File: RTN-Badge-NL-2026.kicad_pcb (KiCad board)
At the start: 2 copper layers, 85.5 x 54 mm, 152 parts, among them J1 USB_A_Edge_Connector, J2 DEBUG, J3 GPIO, SW1 BOOT, SW2 RST, SW3 USER1, SW4 USER2, U1 CH32V203F6P6, U2 ME6211C33M5, Y1 8MHz

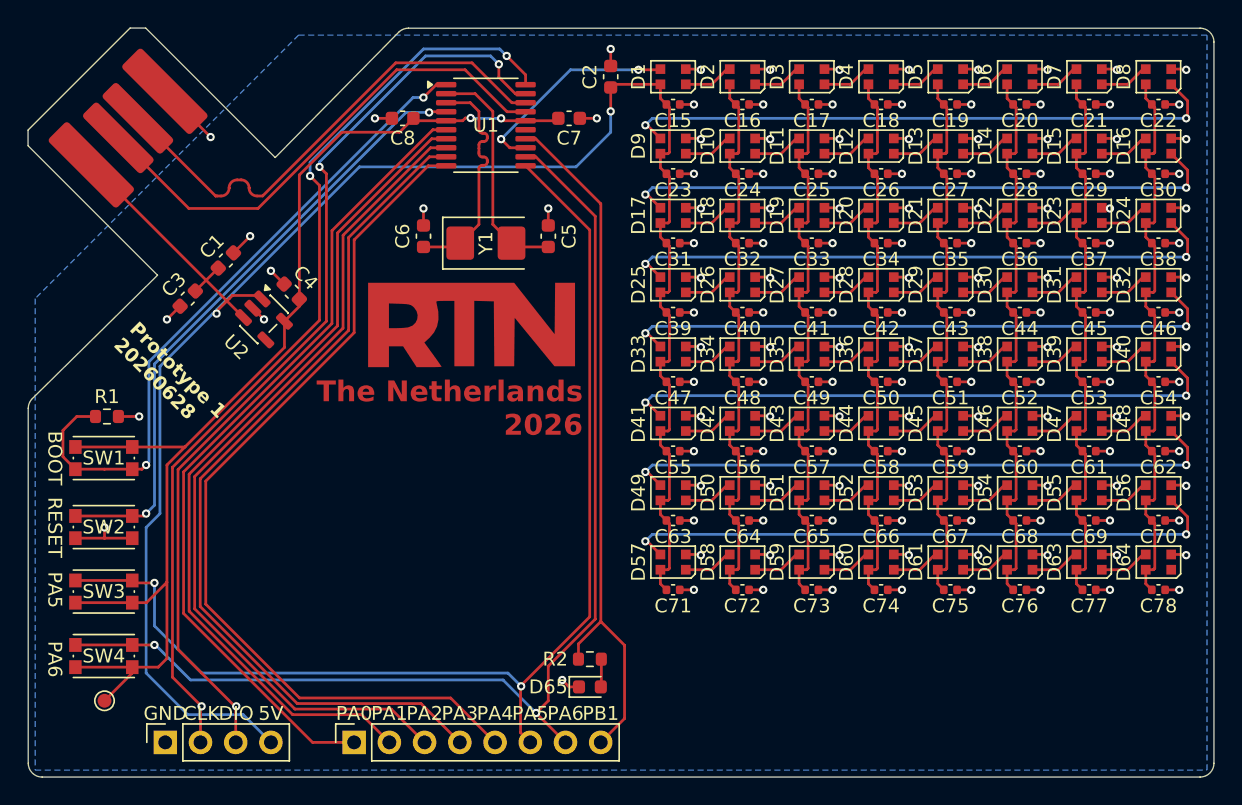
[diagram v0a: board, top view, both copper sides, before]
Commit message: Adjust PCB to use components available in JLCPCB's product library
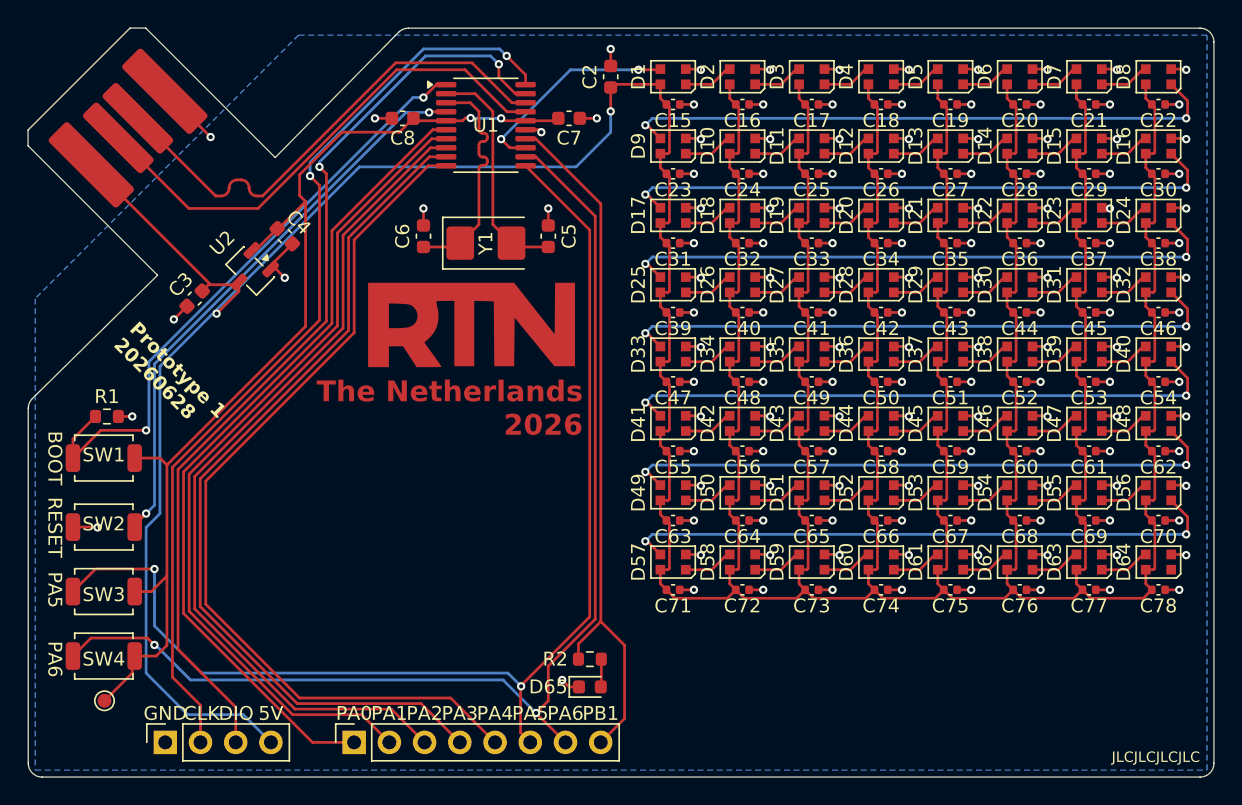
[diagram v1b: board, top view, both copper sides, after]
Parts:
- removed C1: 4.7uF or 10uF, Capacitor_SMD:C_0603_1608Metric
- C7, C8: value 20pF -> 100pF
- SW1, SW2, SW3, SW4: footprint Button_Switch_SMD:SW_Push_1P1T_NO_CK_KMR2 -> Button_Switch_SMD:SW_SPST_TS-1088-xR020
- U2: value ME6211C33M5 -> XC6206PxxxMR; footprint Package_TO_SOT_SMD:SOT-23-5 -> Package_TO_SOT_SMD:SOT-23-3
- moved C4 4.03 mm to (43.5, 40.0), turned to -45 degrees
- moved U2 3.64 mm to (41.0, 42.5), turned to -135 degrees
- moved C3 0.50 mm to (37.0, 44.5)
- turned SW1 to 180 degrees
- turned SW2 to 180 degrees
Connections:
- U2 pad 1: +5V -> GND
- U2 pad 2: GND -> +3V3
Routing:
- net +5V: track 443.3 -> 478.0 mm
- net +3V3: track 85.0 -> 76.0 mm
- net /BOOT: track 48.4 -> 44.5 mm
- net /RST: track 44.8 -> 40.9 mm
- net GND: track 159.7 -> 156.9 mm, vias 141 -> 140
- net /PA5: track 83.0 -> 84.7 mm
- net /PA6: track 82.7 -> 83.7 mm
- net /SWDIO: track 68.0 -> 67.9 mm, vias 3 -> 2
- net /SWCLK: track 67.8 -> 67.7 mm, vias 3 -> 2
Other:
- board text added: "JLCJLCJLCJLC"
